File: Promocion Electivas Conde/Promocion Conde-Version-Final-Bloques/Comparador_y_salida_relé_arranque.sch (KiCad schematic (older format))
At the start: 23 parts, among them K1 DIPxx-1Cxx-51x, Q2 BC848, U5 TL082

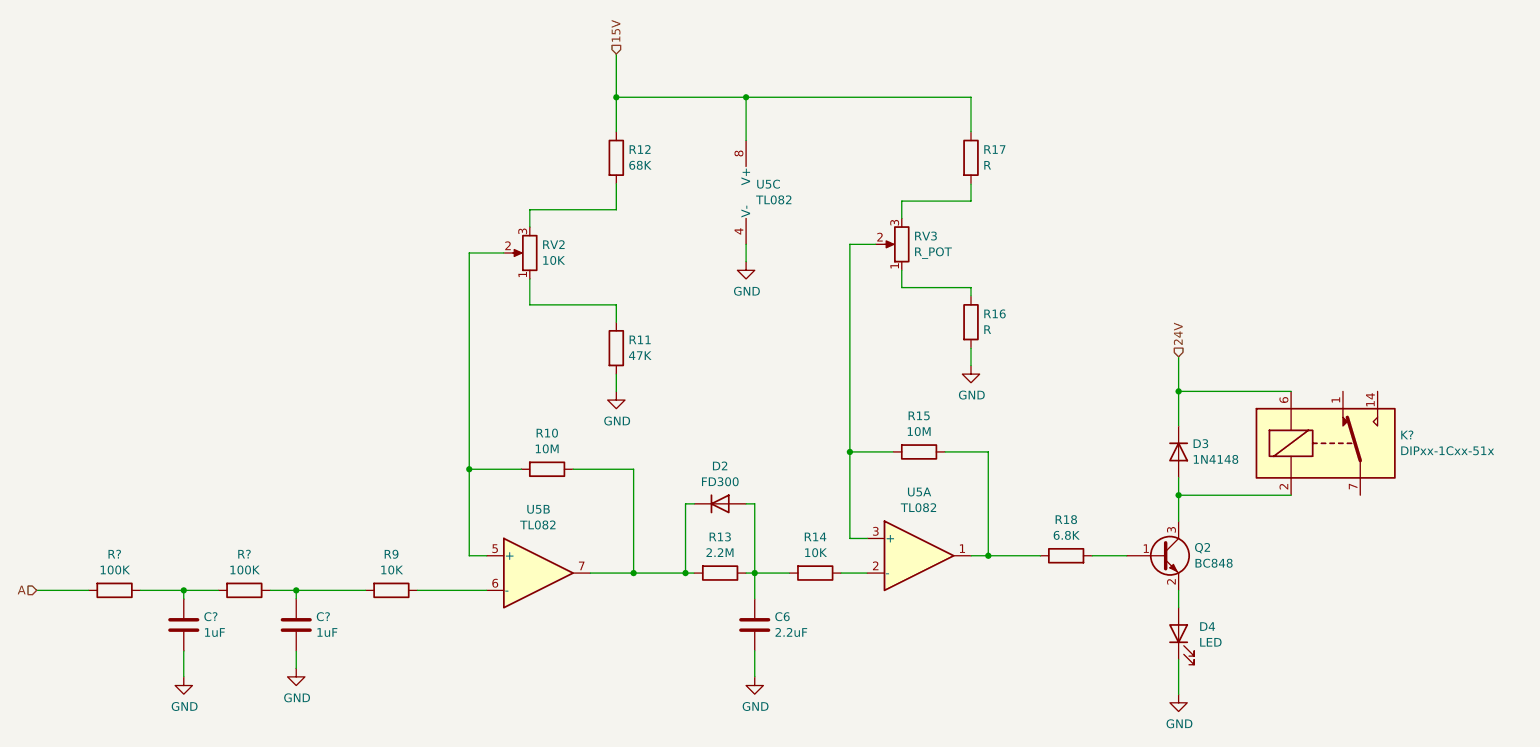
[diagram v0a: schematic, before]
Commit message: Bloques y footprint asignados
Falta elegir y asignar el de los potenciometros Rv3 y Rv7.
Las salidas K3 y K20 también...
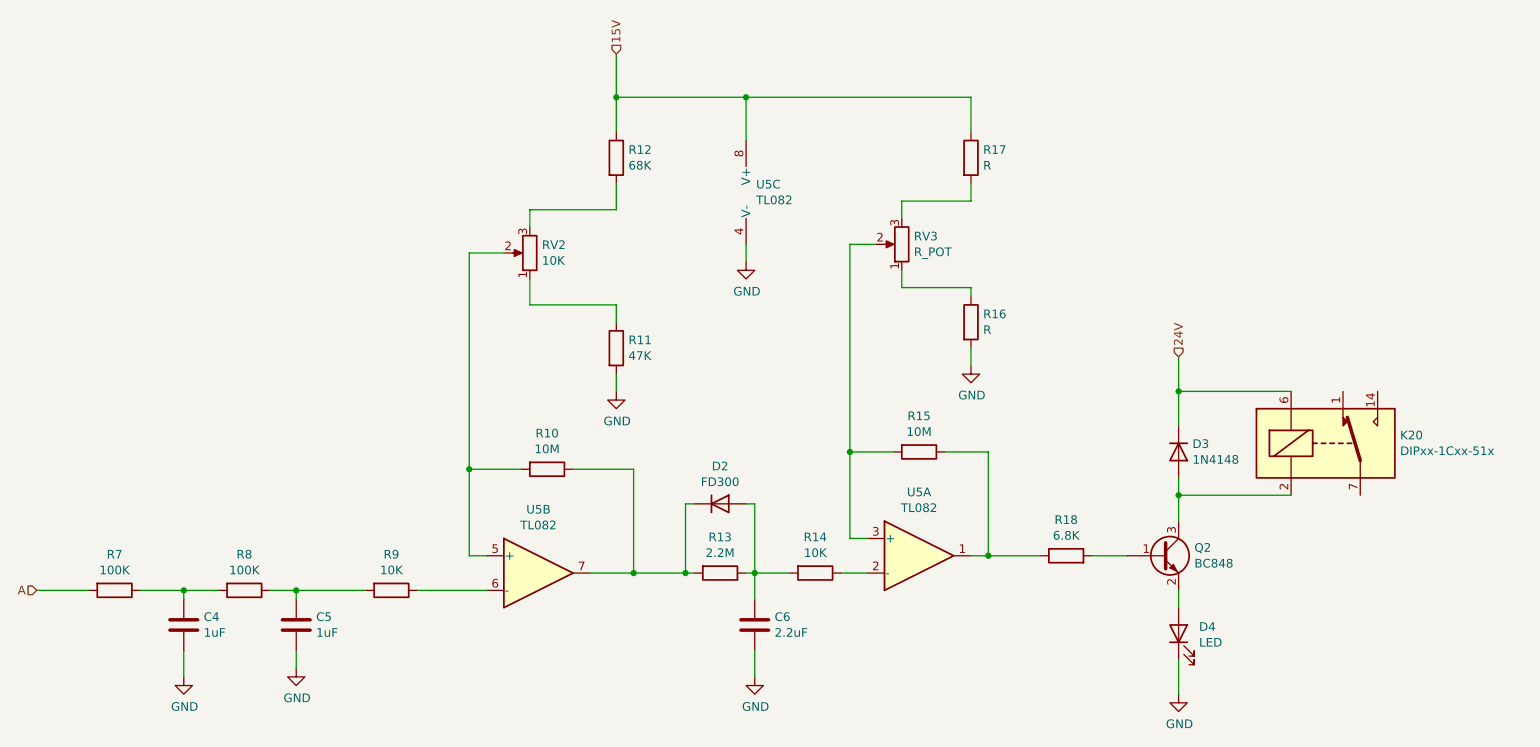
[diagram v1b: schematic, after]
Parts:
- renumbered K1 to K20

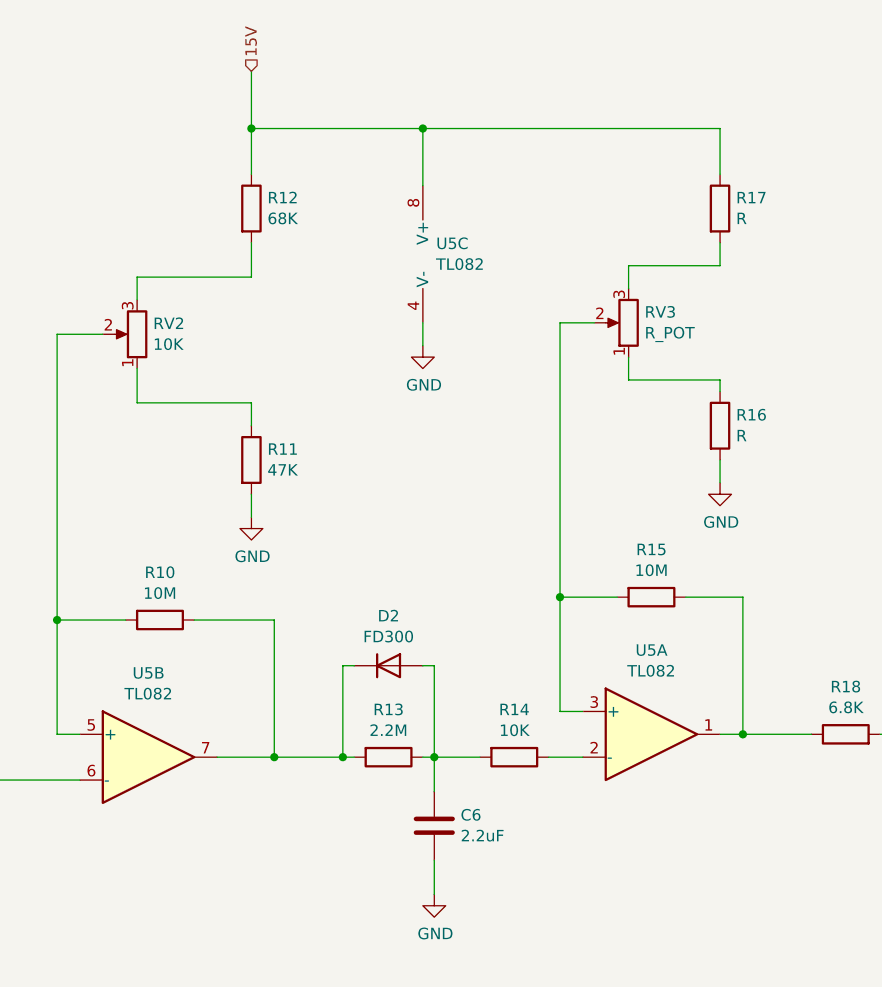
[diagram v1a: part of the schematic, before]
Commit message: Acomode un poco mejor la salida a rele
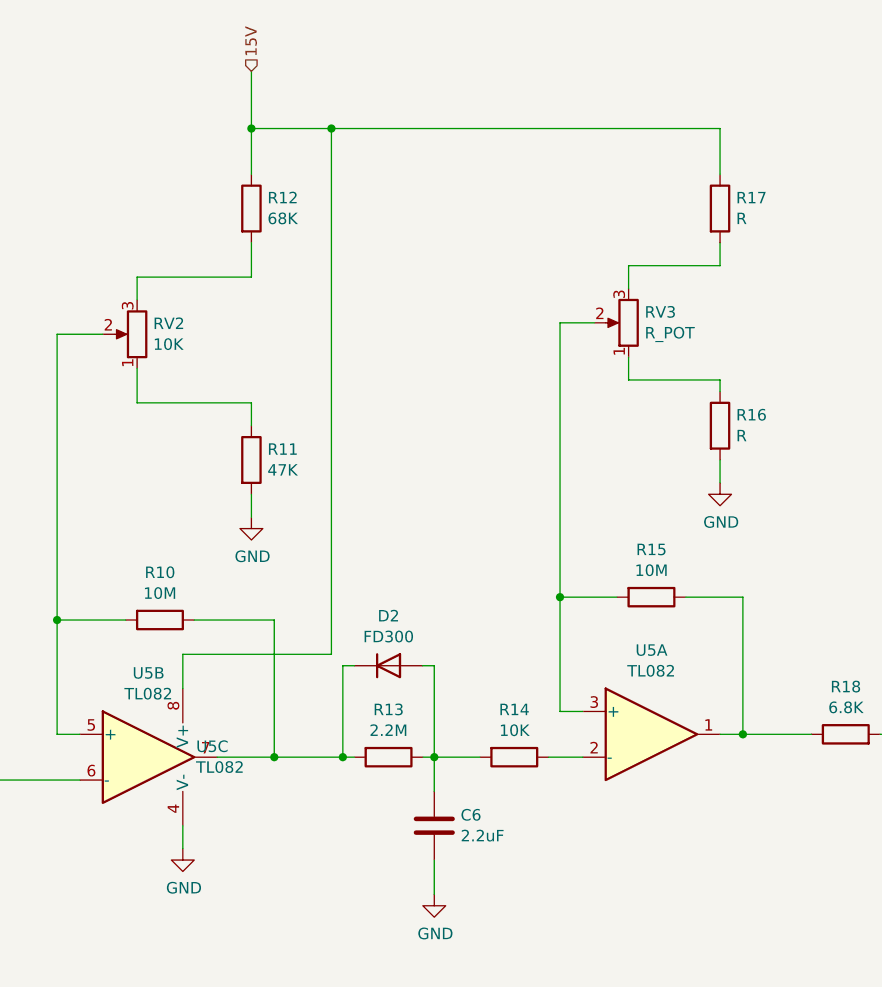
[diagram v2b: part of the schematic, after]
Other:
- moved on the sheet: U5C
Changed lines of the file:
@@
 	4150 1450 4150 1700
-Wire Wire Line
-	4150 1700 4900 1700
 Wire Wire Line
 	6200 1700 6200 1900
@@
 L Amplifier_Operational:TL082 U5
 U 3 1 6137FE67
-P 5000 2250
+P 3950 4450
 AR Path="/61322896/6137FE67" Ref="U5"  Part="3"
 AR Path="/612F0357/6137FE67" Ref="U?"  Part="3"
 AR Path="/618B3478/6137FE67" Ref="U?"  Part="3"
 AR Path="/618B375A/6137FE67" Ref="U?"  Part="3"
-F 0 "U5" H 4958 2296 50  0000 L CNN
-F 1 "TL082" H 4958 2205 50  0000 L CNN
-F 2 "Package_SO:SOIC-8-1EP_3.9x4.9mm_P1.27mm_EP2.29x3mm" H 5000 2250 50  0001 C CNN
-F 3 "https://www.digikey.com/es/products/detail/texas-instruments/TL082CDE4/13472954" H 5000 2250 50  0001 C CNN
-	3    5000 2250
+F 0 "U5" H 3908 4496 50  0000 L CNN
+F 1 "TL082" H 3908 4405 50  0000 L CNN
+F 2 "Package_SO:SOIC-8-1EP_3.9x4.9mm_P1.27mm_EP2.29x3mm" H 3950 4450 50  0001 C CNN
+F 3 "https://www.digikey.com/es/products/detail/texas-instruments/TL082CDE4/13472954" H 3950 4450 50  0001 C CNN
+	3    3950 4450
 	1    0    0    -1
 $EndComp
-Wire Wire Line
-	4900 1950 4900 1700
-Connection ~ 4900 1700
-Wire Wire Line
-	4900 1700 6200 1700
 $Comp
 L power:GND #PWR0121
 U 1 1 6138D593
-P 4900 2650
+P 3850 4850
 AR Path="/61322896/6138D593" Ref="#PWR0121"  Part="1"
 AR Path="/612F0357/6138D593" Ref="#PWR?"  Part="1"
 AR Path="/618B3478/6138D593" Ref="#PWR?"  Part="1"
 AR Path="/618B375A/6138D593" Ref="#PWR?"  Part="1"
-F 0 "#PWR0121" H 4900 2400 50  0001 C CNN
-F 1 "GND" H 4905 2477 50  0000 C CNN
-F 2 "" H 4900 2650 50  0001 C CNN
-F 3 "" H 4900 2650 50  0001 C CNN
-	1    4900 2650
+F 0 "#PWR0121" H 3850 4600 50  0001 C CNN
+F 1 "GND" H 3855 4677 50  0000 C CNN
+F 2 "" H 3850 4850 50  0001 C CNN
+F 3 "" H 3850 4850 50  0001 C CNN
+	1    3850 4850
 	1    0    0    -1
 $EndComp
 Wire Wire Line
-	4900 2650 4900 2550
+	3850 4850 3850 4750
 $Comp
 L Device:R R18
@@
 Wire Wire Line
 	7400 4000 7400 3900
+Wire Wire Line
+	4150 1700 4500 1700
+Wire Wire Line
+	3850 4150 3850 4000
+Wire Wire Line
+	3850 4000 4500 4000
+Wire Wire Line
+	4500 4000 4500 1700
+Connection ~ 4500 1700
+Wire Wire Line
+	4500 1700 6200 1700
 $EndSCHEMATC

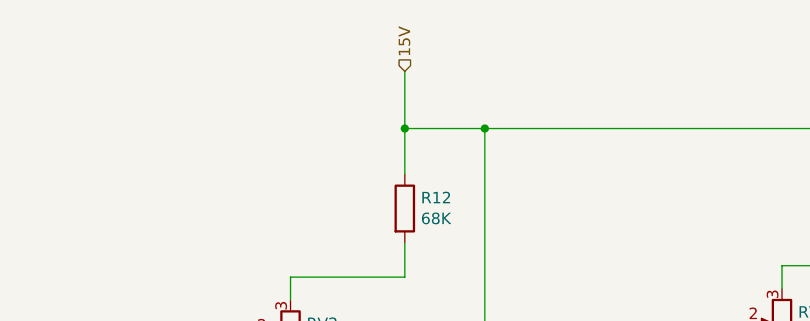
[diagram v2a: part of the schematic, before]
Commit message: Actualizacion Convertidor
Se creó el esquemático del convertidor y se hizo la conexión del mismo
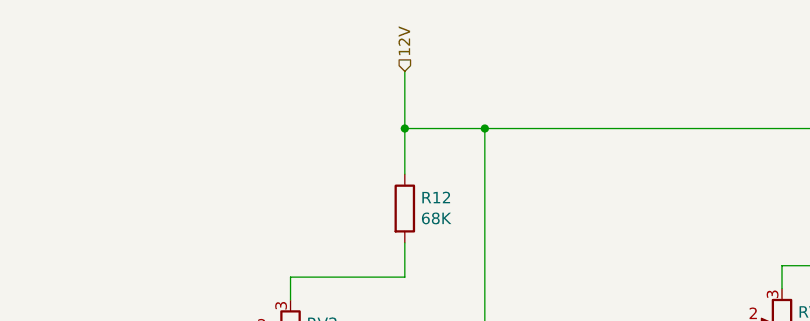
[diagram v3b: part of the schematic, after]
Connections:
- net 15V renamed 12V
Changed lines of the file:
@@
 	4150 3400 4150 3300
 Text HLabel 4150 1450 1    50   Input ~ 0
-15V
+12V
 $Comp
 L Device:R R13

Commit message: Actualizacion
Actualizo los footprints del esquematico y se inicia el PCB
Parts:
- D3: footprint Diode_THT:D_DO-35_SOD27_P7.62mm_Horizontal -> Diode_SMD:D_SOD-323
- D4: footprint Diode_SMD:D_0603_1608Metric_Pad1.05x0.95mm_HandSolder -> LED_SMD:LED_1206_3216Metric
- RV2: footprint Resistor_SMD:R_0603_1608Metric_Pad0.98x0.95mm_HandSolder -> Potentiometer_SMD:Potentiometer_Vishay_TS53YL_Vertical
- RV3: footprint (none) -> Potentiometer_SMD:Potentiometer_Vishay_TS53YL_Vertical
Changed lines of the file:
@@
 F 0 "RV2" H 3580 2554 50  0000 R CNN
 F 1 "10K" H 3580 2645 50  0000 R CNN
-F 2 "Resistor_SMD:R_0603_1608Metric_Pad0.98x0.95mm_HandSolder" H 3650 2600 50  0001 C CNN
-F 3 "~" H 3650 2600 50  0001 C CNN
+F 2 "Potentiometer_SMD:Potentiometer_Vishay_TS53YL_Vertical" H 3650 2600 50  0001 C CNN
+F 3 "https://www.vishay.com/docs/51008/ts53.pdf" H 3650 2600 50  0001 C CNN
 	1    3650 2600
 	-1   0    0    1
@@
 F 0 "RV3" H 5730 2504 50  0000 R CNN
 F 1 "R_POT" H 5730 2595 50  0000 R CNN
-F 2 "" H 5800 2550 50  0001 C CNN
-F 3 "~" H 5800 2550 50  0001 C CNN
+F 2 "Potentiometer_SMD:Potentiometer_Vishay_TS53YL_Vertical" H 5800 2550 50  0001 C CNN
+F 3 "https://www.vishay.com/docs/51008/ts53.pdf" H 5800 2550 50  0001 C CNN
 	1    5800 2550
 	-1   0    0    1
@@
 F 0 "D4" V 7439 4682 50  0000 R CNN
 F 1 "LED" V 7348 4682 50  0000 R CNN
-F 2 "Diode_SMD:D_0603_1608Metric_Pad1.05x0.95mm_HandSolder" H 7400 4800 50  0001 C CNN
-F 3 "~" H 7400 4800 50  0001 C CNN
+F 2 "LED_SMD:LED_1206_3216Metric" H 7400 4800 50  0001 C CNN
+F 3 "https://www.aopled.com/AOP_PDFs/L152L-LIC.pdf" H 7400 4800 50  0001 C CNN
 	1    7400 4800
 	0    -1   -1   0
@@
 F 0 "D3" V 7354 3830 50  0000 L CNN
 F 1 "1N4148" V 7445 3830 50  0000 L CNN
-F 2 "Diode_THT:D_DO-35_SOD27_P7.62mm_Horizontal" H 7400 3575 50  0001 C CNN
-F 3 "https://assets.nexperia.com/documents/data-sheet/1N4148_1N4448.pdf" H 7400 3750 50  0001 C CNN
+F 2 "Diode_SMD:D_SOD-323" H 7400 3575 50  0001 C CNN
+F 3 "https://www.diodes.com/assets/Datasheets/1N4148WSF.pdf" H 7400 3750 50  0001 C CNN
 	1    7400 3750
 	0    1    1    0
